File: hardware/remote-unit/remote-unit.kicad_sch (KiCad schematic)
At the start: 59 parts, among them J1 SOL_A, J2 RF Module, J3 ICSP, J5 SOL_B, J6 PWR 12V, J7 UART, J8 RS485, J9 SOLAR, Q1 N >1A@4VGS, Q2 PNP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

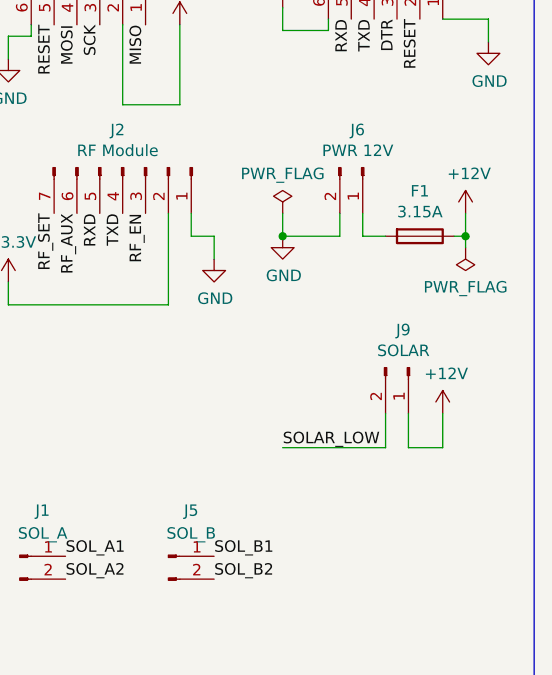
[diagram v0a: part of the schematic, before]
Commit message: Add SMT fuse to remote unit
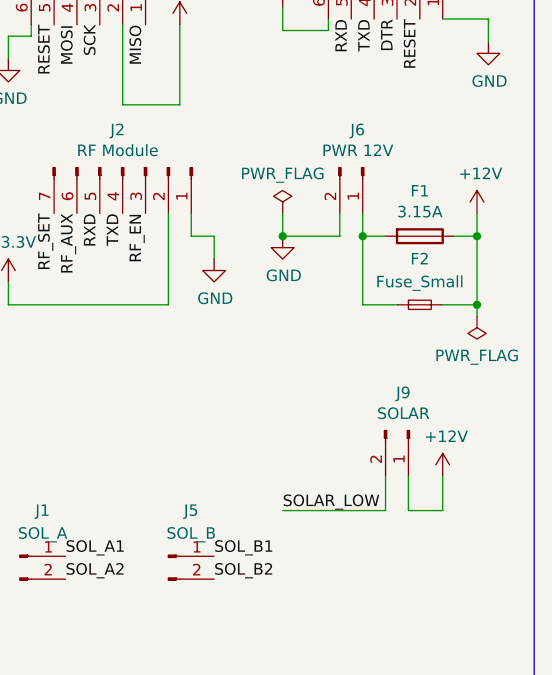
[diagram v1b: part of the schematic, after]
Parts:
- added F2: Fuse_Small, Fuse:Fuse_0603_1608Metric, symbol Device:Fuse_Small
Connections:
- net +12V: now also F2.2
- net at F1.2, J6.1 (Pin_1): now also F2.1
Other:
- moved on the sheet: J9
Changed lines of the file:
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@@
 	)
 	(junction
-		(at 275.59 52.07)
-		(diameter 0)
-		(color 0 0 0 0)
-	)
-	(junction
 		(at 173.99 24.13)
 		(diameter 0)
@@
 	)
 	(junction
+		(at 276.86 52.07)
+		(diameter 0)
+		(color 0 0 0 0)
+	)
+	(junction
 		(at 69.85 170.18)
 		(diameter 0)
@@
 	)
 	(junction
+		(at 276.86 59.69)
+		(diameter 0)
+		(color 0 0 0 0)
+	)
+	(junction
 		(at 177.8 44.45)
 		(diameter 0)
@@
 	)
 	(junction
+		(at 264.16 52.07)
+		(diameter 0)
+		(color 0 0 0 0)
+	)
+	(junction
 		(at 231.14 111.76)
 		(diameter 0)
@@
 	(wire
 		(pts
+			(xy 276.86 59.69) (xy 276.86 52.07)
+		)
+		(stroke
+			(width 0)
+			(type default)
+		)
+	)
+	(wire
+		(pts
 			(xy 231.14 111.76) (xy 254 111.76)
 		)
@@
 	(wire
 		(pts
-			(xy 269.24 75.565) (xy 273.05 75.565)
+			(xy 269.24 82.55) (xy 273.05 82.55)
 		)
 		(stroke
@@
 	(wire
 		(pts
-			(xy 266.7 75.565) (xy 255.27 75.565)
+			(xy 266.7 82.55) (xy 255.27 82.55)
 		)
 		(stroke
@@
 	(wire
 		(pts
-			(xy 275.59 53.34) (xy 275.59 52.07)
+			(xy 276.86 60.96) (xy 276.86 59.69)
 		)
 		(stroke
@@
 		)
 	)
+	(wire
+		(pts
+			(xy 273.05 59.69) (xy 276.86 59.69)
+		)
+		(stroke
+			(width 0)
+			(type default)
+		)
+	)
 	(polyline
 		(pts
@@
 	(wire
 		(pts
-			(xy 273.05 75.565) (xy 273.05 71.755)
+			(xy 273.05 82.55) (xy 273.05 78.74)
 		)
 		(stroke
@@
 	(wire
 		(pts
+			(xy 267.97 59.69) (xy 264.16 59.69)
+		)
+		(stroke
+			(width 0)
+			(type default)
+		)
+	)
+	(wire
+		(pts
 			(xy 132.08 49.53) (xy 132.08 50.8)
 		)
@@
 	(wire
 		(pts
-			(xy 275.59 49.53) (xy 275.59 52.07)
+			(xy 276.86 49.53) (xy 276.86 52.07)
 		)
 		(stroke
@@
 	(wire
 		(pts
-			(xy 275.59 52.07) (xy 274.32 52.07)
+			(xy 274.32 52.07) (xy 276.86 52.07)
 		)
 		(stroke
@@
 	(wire
 		(pts
+			(xy 264.16 52.07) (xy 264.16 59.69)
+		)
+		(stroke
+			(width 0)
+			(type default)
+		)
+	)
+	(wire
+		(pts
 			(xy 122.555 135.255) (xy 122.555 139.7)
 		)
@@
 	(wire
 		(pts
-			(xy 266.7 71.755) (xy 266.7 75.565)
+			(xy 266.7 78.74) (xy 266.7 82.55)
 		)
 		(stroke
@@
 	(wire
 		(pts
-			(xy 269.24 71.755) (xy 269.24 75.565)
+			(xy 269.24 78.74) (xy 269.24 82.55)
 		)
 		(stroke
@@
 	)
 	(label "SOLAR_LOW"
-		(at 255.27 75.565 0)
+		(at 255.27 82.55 0)
 		(effects
 			(font
@@
 	(symbol
 		(lib_id "power:+12V")
-		(at 275.59 49.53 0)
+		(at 276.86 49.53 0)
 		(unit 1)
 		(exclude_from_sim no)
@@
 		(dnp no)
 		(property "Reference" "#PWR031"
-			(at 275.59 53.34 0)
+			(at 276.86 53.34 0)
 			(effects
 				(font
@@
 		)
 		(property "Value" "+12V"
-			(at 275.971 45.1358 0)
+			(at 277.241 45.1358 0)
 			(effects
 				(font
@@
 		)
 		(property "Footprint" ""
-			(at 275.59 49.53 0)
+			(at 276.86 49.53 0)
 			(effects
 				(font
@@
 		)
 		(property "Datasheet" ""
-			(at 275.59 49.53 0)
+			(at 276.86 49.53 0)
 			(effects
 				(font
@@
 		)
 		(property "Description" ""
-			(at 275.59 49.53 0)
+			(at 276.86 49.53 0)
 			(effects
 				(font
@@
 	(symbol
 		(lib_id "Connector:Conn_01x02_Pin")
-		(at 269.24 66.675 270)
+		(at 269.24 73.66 270)
 		(unit 1)
 		(exclude_from_sim no)
@@
 		(dnp no)
 		(property "Reference" "J9"
-			(at 268.6812 62.484 90)
+			(at 268.6812 69.469 90)
 			(effects
 				(font
@@
 		)
 		(property "Value" "SOLAR"
-			(at 268.6812 64.7954 90)
+			(at 268.6812 71.7804 90)
 			(effects
 				(font
@@
 		)
 		(property "Footprint" "Connector_JST:JST_XH_B2B-XH-A_1x02_P2.50mm_Vertical"
-			(at 269.24 66.675 0)
+			(at 269.24 73.66 0)
 			(effects
 				(font
@@
 		)
 		(property "Datasheet" "~"
-			(at 269.24 66.675 0)
+			(at 269.24 73.66 0)
 			(effects
 				(font
@@
 		)
 		(property "Description" ""
-			(at 269.24 66.675 0)
+			(at 269.24 73.66 0)
 			(effects
 				(font
@@
 		)
 		(property "Purchase Link" "https://au.mouser.com/ProductDetail/426-FIT0255"
-			(at 269.24 66.675 90)
+			(at 269.24 73.66 90)
 			(effects
 				(font
@@
 	(symbol
 		(lib_id "power:PWR_FLAG")
-		(at 275.59 53.34 180)
+		(at 276.86 60.96 180)
 		(unit 1)
 		(exclude_from_sim no)
@@
 		(dnp no)
 		(property "Reference" "#FLG04"
-			(at 275.59 55.245 0)
+			(at 276.86 62.865 0)
 			(effects
 				(font
@@
 		)
 		(property "Value" "PWR_FLAG"
-			(at 275.59 57.7342 0)
+			(at 276.86 65.3542 0)
 			(effects
 				(font
@@
 		)
 		(property "Footprint" ""
-			(at 275.59 53.34 0)
+			(at 276.86 60.96 0)
 			(effects
 				(font
@@
 		)
 		(property "Datasheet" "~"
-			(at 275.59 53.34 0)
+			(at 276.86 60.96 0)
 			(effects
 				(font
@@
 		)
 		(property "Description" ""
-			(at 275.59 53.34 0)
+			(at 276.86 60.96 0)
 			(effects
 				(font
@@
 	(symbol
 		(lib_id "power:+12V")
-		(at 273.05 71.755 0)
+		(at 273.05 78.74 0)
 		(unit 1)
 		(exclude_from_sim no)
@@
 		(dnp no)
 		(property "Reference" "#PWR033"
-			(at 273.05 75.565 0)
+			(at 273.05 82.55 0)
 			(effects
 				(font
@@
 		)
 		(property "Value" "+12V"
-			(at 273.431 67.3608 0)
+			(at 273.431 74.3458 0)
 			(effects
 				(font
@@
 		)
 		(property "Footprint" ""
-			(at 273.05 71.755 0)
+			(at 273.05 78.74 0)
 			(effects
 				(font
@@
 		)
 		(property "Datasheet" ""
-			(at 273.05 71.755 0)
+			(at 273.05 78.74 0)
 			(effects
 				(font
@@
 		)
 		(property "Description" ""
-			(at 273.05 71.755 0)
+			(at 273.05 78.74 0)
 			(effects
 				(font
@@
 					(unit 1)
 				)
+			)
+		)
+	)
+	(symbol
+		(lib_id "Device:Fuse_Small")
+		(at 270.51 59.69 0)
+		(unit 1)
+		(exclude_from_sim no)
+		(in_bom yes)
+		(on_board yes)
+		(dnp no)
+		(fields_autoplaced yes)
+		(property "Reference" "F2"
+			(at 270.51 54.61 0)
+			(effects
+				(font
+					(size 1.27 1.27)
+				)
+			)
+		)
+		(property "Value" "Fuse_Small"
+			(at 270.51 57.15 0)
+			(effects
+				(font
+					(size 1.27 1.27)
+				)
+			)
+		)
+		(property "Footprint" "Fuse:Fuse_0603_1608Metric"
+			(at 270.51 59.69 0)
+			(effects
+				(font
+					(size 1.27 1.27)
+				)
+				(hide yes)
+			)
+		)
+		(property "Datasheet" "https://www.lcsc.com/datasheet/C163117.pdf"
+			(at 270.51 59.69 0)
+			(effects
+				(font
+					(size 1.27 1.27)
+				)
+				(hide yes)
+			)
+		)
+		(property "Description" "Fuse, small symbol"
+			(at 270.51 59.69 0)
+			(effects
+				(font
+					(size 1.27 1.27)
+				)
+				(hide yes)
+			)
+		)
+		(property "JLCPCB Part" "C163117"
+			(at 270.51 59.69 0)
+			(effects
+				(font
+					(size 1.27 1.27)
+				)
+				(hide yes)
+			)
+		)
+		(pin "2"
+		)
+		(pin "1"
+		)
+		(instances
+			(project ""
+				(path "/18be3b1b-9bcf-4c4f-bb2a-ca2504ea30e0"
+					(reference "F2")
+					(unit 1)
+				)

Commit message: Use SMT MAX3485 for remote unit
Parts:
- U5: footprint Package_DIP:DIP-8_W7.62mm -> Package_SO:MSOP-8_3x3mm_P0.65mm; JLCPCB Part (none) -> C5310819
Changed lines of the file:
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@@
 			)
 		)
-		(property "Footprint" "Package_DIP:DIP-8_W7.62mm"
+		(property "Footprint" "Package_SO:MSOP-8_3x3mm_P0.65mm"
 			(at 122.555 170.18 0)
 			(effects
@@
 			)
 		)
-		(property "Datasheet" "https://datasheets.maximintegrated.com/en/ds/MAX3483-MAX3491.pdf"
+		(property "Datasheet" "https://xonstorage.z8.web.core.windows.net/pdf/hgsemi_max3485ecmmtr_apr22_xonlink.pdf"
 			(at 122.555 151.13 0)
 			(effects
@@
 			)
 		)
+		(property "JLCPCB Part" "C5310819"
+			(at 122.555 152.4 0)
+			(effects
+				(font
+					(size 1.27 1.27)
+				)
+				(hide yes)
+			)
+		)

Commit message: Add remote unit current sense resistors
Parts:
- added R14, R15: 100m, Resistor_SMD:R_2512_6332Metric, symbol Device:R
- J1: value SOL_A -> SLND_A
- J5: value SOL_B -> SLND_B
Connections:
- net GND: now also R14.2, R15.2; no longer U2.7 (ISEN), U3.7 (ISEN)
- net ADC6: now reaches U1.19 (ADC6)
- net ADC6: now also U2.7 (ISEN), R14.1
- net ADC7: now reaches U1.22 (ADC7)
- net ADC7: now also U3.7 (ISEN), R15.1
- no-connect marks 3 -> 1
